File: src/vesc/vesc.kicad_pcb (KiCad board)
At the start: 6 copper layers, 72.8 x 100 mm, 158 parts, among them J1 Conn_01x02, J101 USB_C_Receptacle_USB2.0_16P, J2 Conn_01x03, J3 Conn_01x02, J7 Conn_02x03_Odd_Even, P4 HALL/Encoder, Q1 NCEP60T20, Q2 NCEP60T20, Q3 NCEP60T20, Q4 NCEP60T20, Q5 NCEP60T20, Q6 NCEP60T20, U1 HX4002, U2 DRV8301, U3 TCAN1462V, U3A1 TP2604-SR, U3B1 TP2604-SR, U3C1 TP2604-SR, U5 STM32F405RGT6, X1 24MHz

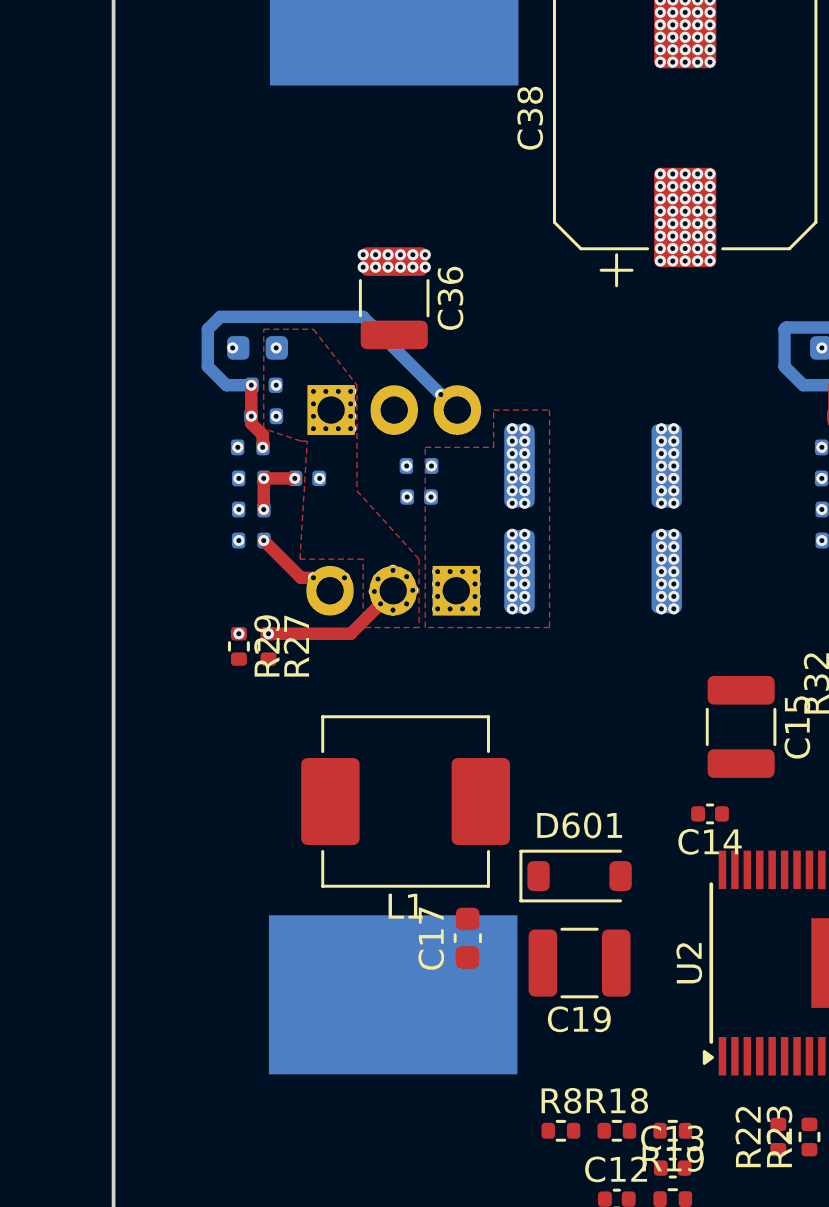
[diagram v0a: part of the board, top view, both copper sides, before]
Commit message: new mosfet planes
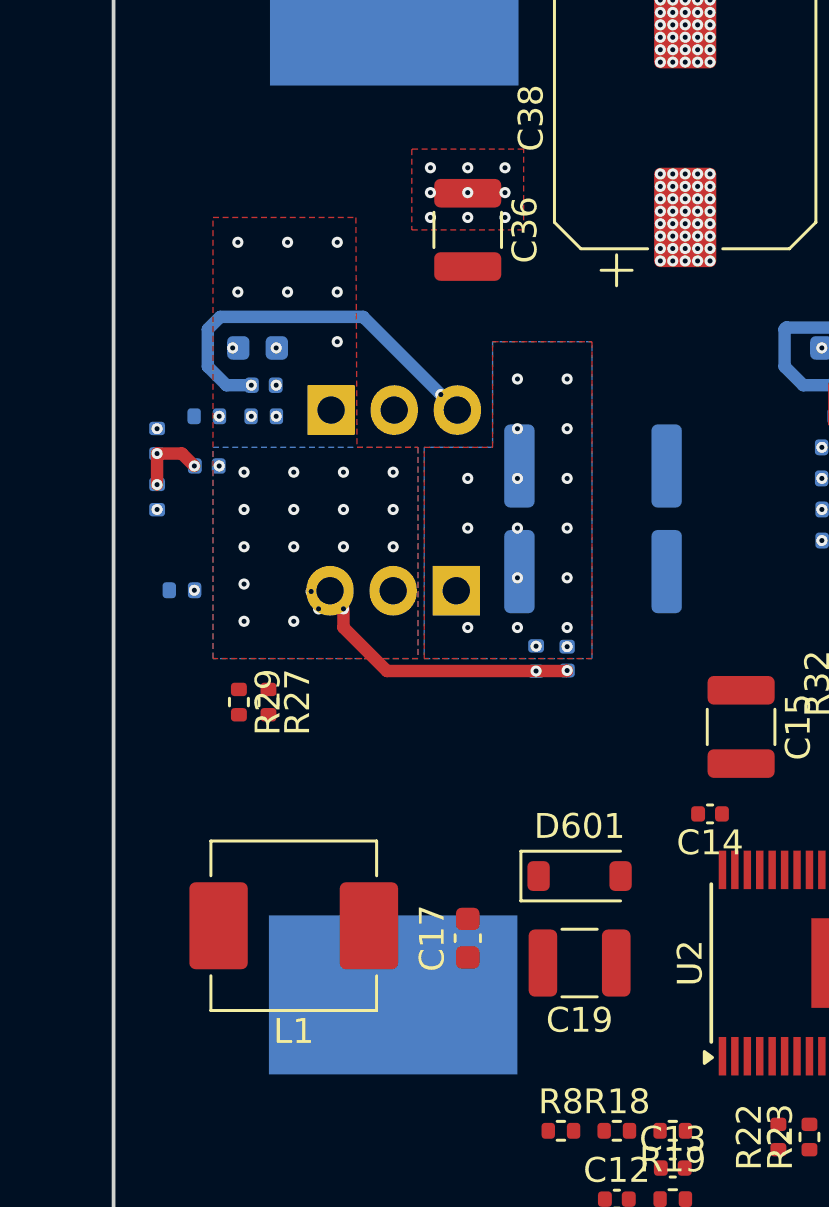
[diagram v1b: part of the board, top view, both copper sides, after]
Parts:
- moved R50 9.07 mm to (124.2, 90.2), turned to 90 degrees
- moved C62 8.82 mm to (125.5, 90.2), turned to 90 degrees
- moved L1 6.73 mm to (114.5, 101.0)
- moved R33 4.08 mm to (109.0, 81.5), turned to -90 degrees
- moved C40 4.07 mm to (111.0, 82.5)
- moved C36 4.04 mm to (121.5, 73.0)
- moved R53 3.83 mm to (109.0, 83.8), turned to 90 degrees
- moved R47 3.43 mm to (110.0, 87.5)
- moved R27 2.24 mm to (113.5, 92.0)
- moved R29 2.24 mm to (112.3, 92.0)
- moved R41 2.15 mm to (111.0, 80.5)
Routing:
- net Net-(Q4-G): track 8.17 -> 15.2 mm, vias 5 -> 6
- net /Mosfet driver/H1_VS: track 5.01 -> 0.00 mm, vias 25 -> 26
- net Net-(Q1-G): track 17.3 -> 14.6 mm
- net SNA: vias 42 -> 17
- net GND: vias 226 -> 194
- net /Mosfet driver/GL_A: vias 1 -> 0
- net /Mosfet driver/GH_A: vias 1 -> 0
- added copper zone on B.Cu, net /Mosfet driver/H1_VS
- added copper zone on F.Cu, net GND
- added copper zone on B.Cu, net SNA
- removed copper zone on In3.Cu, net SNA
- removed copper zone on In3.Cu, net SNB
- removed copper zone on In3.Cu, net SNC

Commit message: mosfet passives
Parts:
- R27, R29: moved to B.Cu
- moved R27 2.33 mm to (111.9, 90.2)
- moved R29 2.18 mm to (110.2, 91.2), turned to 90 degrees
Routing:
- net Net-(Q1-G): track 14.6 -> 17.2 mm
- net /MCU/SENS1: track 0.00 -> 1.75 mm
- net V_SUPPLY: vias 81 -> 1
- net GND: vias 194 -> 115

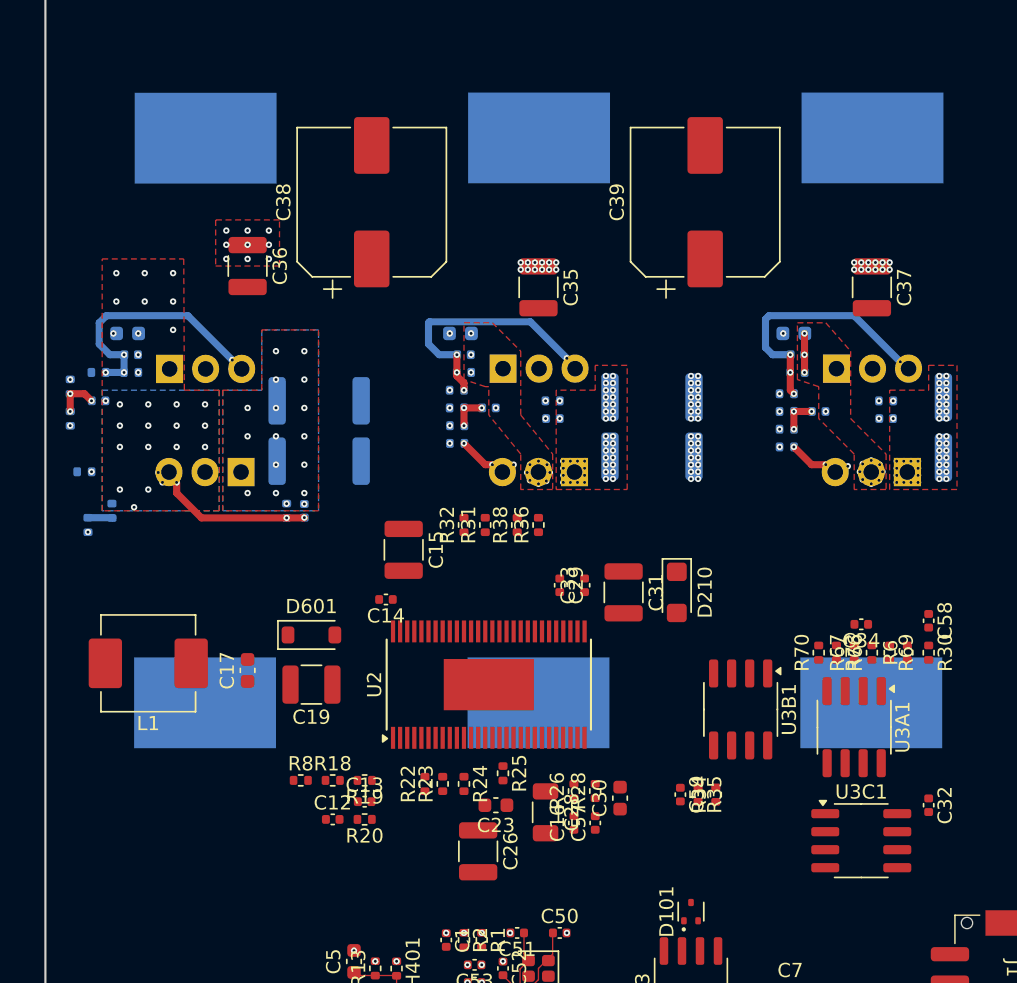
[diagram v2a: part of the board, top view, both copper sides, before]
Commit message: mosfet/capacitor passives, zones, and vias
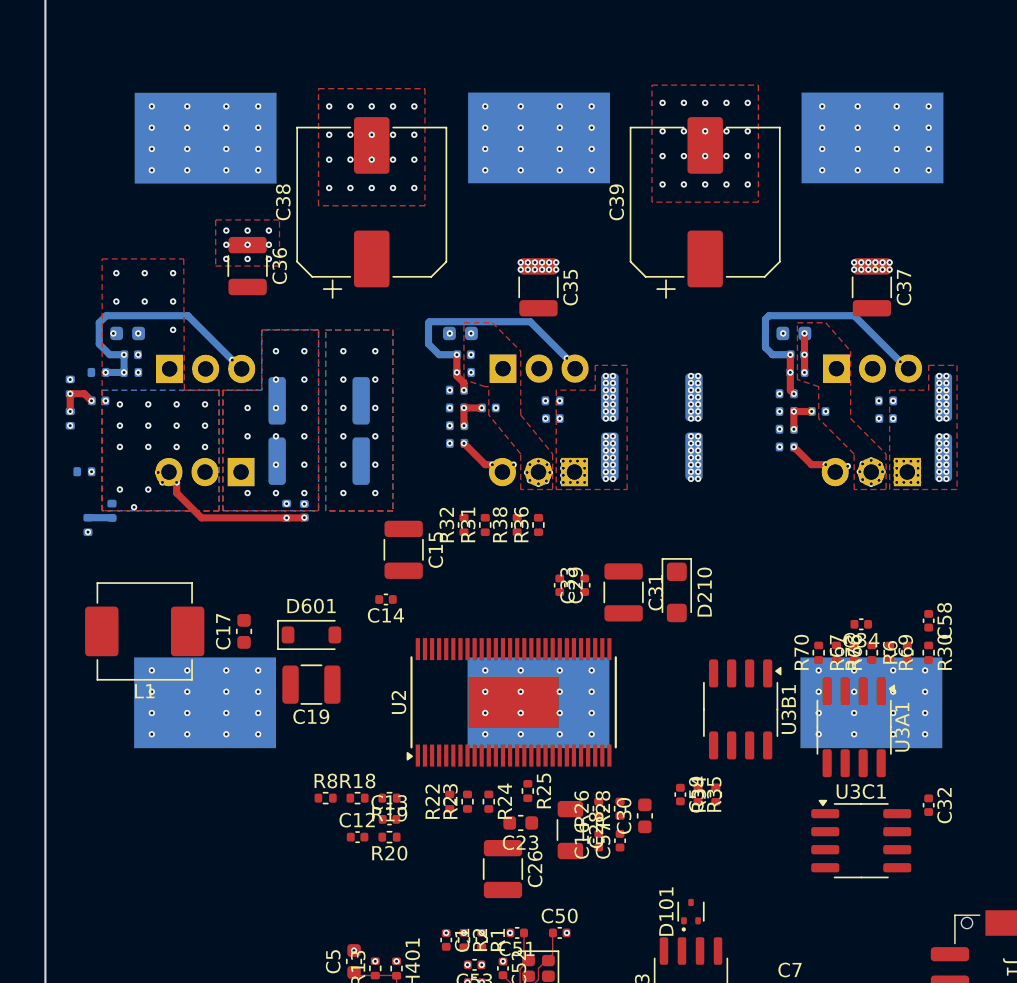
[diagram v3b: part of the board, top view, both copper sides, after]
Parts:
- moved C17 2.76 mm to (121.2, 98.8)
- moved L1 2.26 mm to (114.2, 98.8)
- moved C12 2.15 mm to (129.2, 113.2)
- moved C13 2.15 mm to (131.5, 112.0)
- moved C16 2.15 mm to (146.2, 113.5)
- moved C23 2.15 mm to (140.8, 112.2)
- moved C26 2.15 mm to (139.5, 115.5)
- moved C28 2.15 mm to (144.2, 112.8)
- moved C30 2.15 mm to (149.5, 111.8)
- moved C57 2.15 mm to (147.8, 113.5)
- moved R18 2.15 mm to (129.2, 110.5)
- moved R19 2.15 mm to (131.5, 110.5)
- moved R20 2.15 mm to (131.5, 113.2)
- moved R22 2.15 mm to (135.8, 110.8)
- moved R23 2.15 mm to (137.0, 110.8)
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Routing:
- net GND: vias 115 -> 263
- added copper zone on B.Cu, net GND

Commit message: remaining mosfet zones
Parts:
- moved R51 9.36 mm to (148.2, 90.2), turned to -90 degrees
- moved R52 9.36 mm to (171.8, 90.2), turned to -90 degrees
- moved C67 9.19 mm to (173.0, 90.2), turned to 90 degrees
- moved C65 9.16 mm to (149.5, 90.2), turned to 90 degrees
- moved C41 4.04 mm to (134.5, 83.5)
- moved C37 4.04 mm to (169.2, 73.0)
- moved R37 3.80 mm to (132.5, 84.8), turned to 90 degrees
- moved R54 3.78 mm to (132.5, 82.5), turned to -90 degrees
- moved C35 3.58 mm to (145.2, 73.0)
- moved C42 3.54 mm to (158.2, 83.8)
- moved R48 3.42 mm to (133.5, 87.5)
- moved R39 3.34 mm to (156.2, 82.5), turned to -90 degrees
- moved R55 3.34 mm to (156.2, 85.2), turned to 90 degrees
- moved R49 3.05 mm to (157.0, 87.5)
- moved R31 2.93 mm to (137.2, 94.0)
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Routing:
- net Net-(Q5-G): track 8.05 -> 15.3 mm
- net Net-(Q6-G): track 8.49 -> 15.3 mm
- net /Mosfet driver/H3_VS: track 2.75 -> 0.00 mm, vias 12 -> 24
- net Net-(C42-Pad2): track 2.50 -> 3.56 mm
- net Net-(Q2-G): track 17.4 -> 17.9 mm
- net Net-(Q4-G): track 15.2 -> 15.7 mm
- net SNC: vias 42 -> 16
- net SNB: vias 42 -> 17
- net Net-(U2-BST_C): vias 1 -> 0
- net Net-(U2-BST_B): vias 1 -> 0
- net Net-(U2-BST_A): vias 1 -> 0
- net GND: vias 263 -> 225
- net /Mosfet driver/H2_VS: vias 12 -> 24
- net /Mosfet driver/H1_VS: vias 26 -> 24
- net /Mosfet driver/GL_B: vias 1 -> 0
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- added copper zone on B.Cu, net /Mosfet driver/H2_VS
- added copper zone on B.Cu, net /Mosfet driver/H3_VS
- added copper zone on B.Cu, net SNB
- added copper zone on B.Cu, net SNC

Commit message: fixed weird opamp footprint
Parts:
- removed U3A1, U3B1, U3C1: TP2604-SR, Package_SO:SOP-8_3.76x4.96mm_P1.27mm
- added U4: TP2604-SR, Package_SO:SOIC-8_3.9x4.9mm_P1.27mm, F.Cu at (175.5, 103.3)

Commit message: more component placement
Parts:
- removed H4: Open Hardware Logo, Symbol:OSHW-Logo2_9.8x8mm_SilkScreen
- removed H9: KiCAD Logo, Symbol:KiCad-Logo2_5mm_SilkScreen
- removed X1: 24MHz, Crystal:Crystal_SMD_2016-4Pin_2.0x1.6mm
- added R5: 470R, Resistor_SMD:R_0402_1005Metric, B.Cu at (125.8, 129.2)
- added Y1: Crystal_GND24_Small, Crystal:Crystal_SMD_2016-4Pin_2.0x1.6mm, B.Cu at (125.2, 127.0)
- C1, C12, C13, C14, C15, C16, C17, C19, C2, C201, C23, C29, C3, C30, C31, C32, C33, C34, C4, C45, C46, C47, C48, C49, C5, C50, C51, C52, C53, C55, C56, C57, C58, C59, C7, C9, D101, D210, D501, D601, L1, R1, R13, R18, R19, R2, R20, R22, R23, R24, R25, R26, R28, R30, R31, R32, R34, R35, R36, R38, R501, R6, R66, R67, R69, R70, R73, R8, TH401, U1, U2, U3, U5: moved to B.Cu
- C26: footprint Capacitor_SMD:C_1210_3225Metric -> Capacitor_SMD:C_1206_3216Metric; moved to B.Cu
- C28: footprint Capacitor_SMD:C_1206_3216Metric -> Capacitor_SMD:C_0603_1608Metric; moved to B.Cu
- J7: footprint Connector_PinHeader_1.27mm:PinHeader_2x03_P1.27mm_Vertical_SMD -> Bluesat:IDC6
- U4: footprint Package_SO:SOIC-8_3.9x4.9mm_P1.27mm -> Package_SO:SOP-8_3.76x4.96mm_P1.27mm; moved to B.Cu
- moved D210 132.0 mm to (28.8, 48.0), turned to 180 degrees
- moved J7 34.6 mm to (117.0, 136.8)
- moved C31 34.0 mm to (118.5, 113.0), turned to 90 degrees
- moved C30 31.1 mm to (120.0, 121.5), turned to 0 degrees
- moved D501 30.9 mm to (120.8, 137.2), turned to 0 degrees
- moved C1 28.5 mm to (144.5, 147.5)
- moved C33 28.3 mm to (120.8, 109.8), turned to 180 degrees
- moved R2 27.8 mm to (143.2, 147.5)
- moved R501 27.5 mm to (120.8, 141.5), turned to 180 degrees
- moved U4 27.4 mm to (150.5, 114.5), turned to 180 degrees
- moved R1 27.3 mm to (142.0, 147.5)
- moved C48 26.4 mm to (121.5, 133.5)
- moved C29 26.2 mm to (120.8, 108.5), turned to 0 degrees
- moved C32 24.5 mm to (145.0, 112.5), turned to 0 degrees
- moved C57 24.1 mm to (129.2, 129.0), turned to -90 degrees
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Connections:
- C50 pad 1: Net-(U5-PH0-OSC_IN) -> Net-(C50-Pad1)
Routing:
- net VCC: track 13.0 -> 2.27 mm, vias 9 -> 4
- net GND: track 9.12 -> 0.00 mm, vias 225 -> 217
- net /MCU/ADC_TEMP: track 8.45 -> 0.57 mm
- net Net-(U5-PH0-OSC_IN): track 6.05 -> 0.00 mm
- net Net-(U4B--): track 0.00 -> 5.60 mm
- net Net-(U4A--): track 0.00 -> 5.28 mm
- net Net-(U5-PH1-OSC_OUT): track 5.28 -> 0.06 mm
- net Net-(U4A-+): track 0.00 -> 5.22 mm
- net Net-(R30-Pad2): track 0.00 -> 4.67 mm
- net Net-(U5-VCAP1): track 3.68 -> 0.00 mm
- net NRST: track 2.64 -> 0.00 mm
- net Net-(U5-VCAP2): track 2.68 -> 0.35 mm, vias 1 -> 0
- net SNC: track 0.00 -> 1.59 mm
- net /MCU/BR_SO3: track 0.00 -> 1.51 mm
- net Net-(R6-Pad2): track 0.00 -> 1.50 mm
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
